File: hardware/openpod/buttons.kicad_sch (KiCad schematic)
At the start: 8 parts

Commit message: update power and audio
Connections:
- net at clickwheel-connector1.1 (VDD): now also MPR1.20 (VDD); no longer MPR1.7 (REXT)
- net at clickwheel-connector1.2 (IRQ): now also MPR1.1 (~{IRQ}); no longer MPR1.6 (VSS)
- net at clickwheel-connector1.3 (SCL): now also MPR1.2 (SCL); no longer MPR1.5 (VREG)
- net at clickwheel-connector1.4 (SDA): now also MPR1.3 (SDA); no longer MPR1.4 (ADDR)
- net at clickwheel-connector1.5 (ADDR): now also MPR1.4 (ADDR); no longer MPR1.3 (SDA)
- net at clickwheel-connector1.6 (VREG): now also MPR1.5 (VREG); no longer MPR1.2 (SCL)
- net at clickwheel-connector1.7 (VSS): now also MPR1.6 (VSS); no longer MPR1.1 (~{IRQ})
- net at clickwheel-connector1.8 (REXT): now also MPR1.7 (REXT); no longer MPR1.20 (VDD)

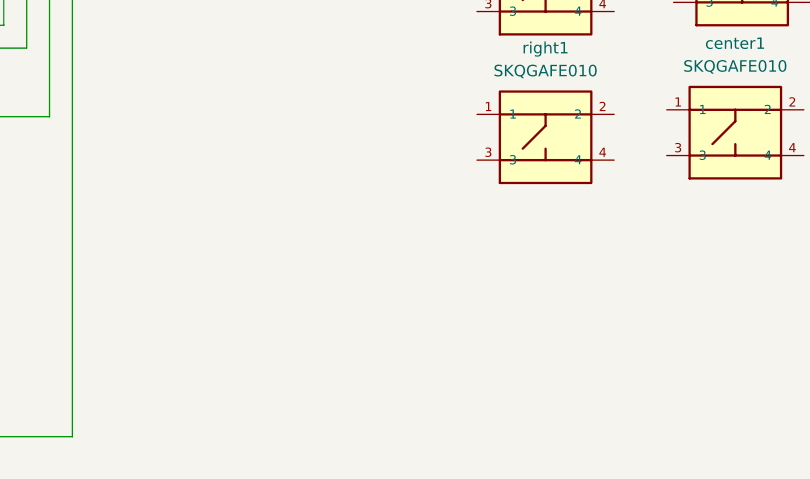
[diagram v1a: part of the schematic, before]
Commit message: added bluetooth
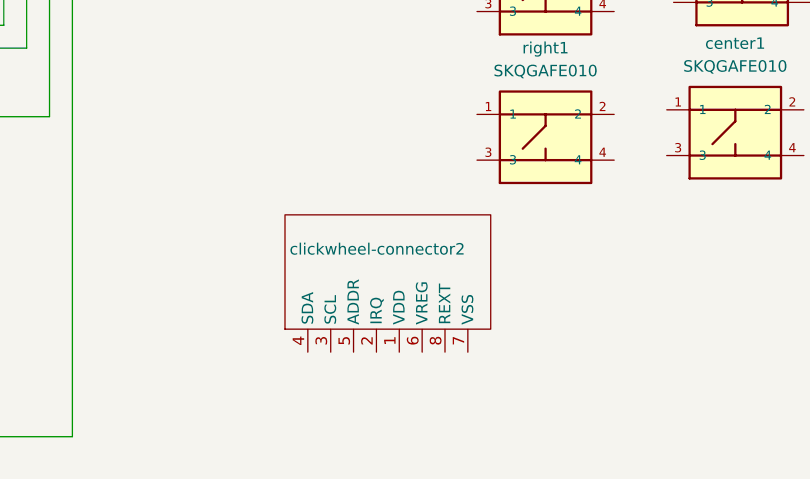
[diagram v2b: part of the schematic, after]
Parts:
- added clickwheel-connector2: ~, Connector_FFC-FPC:Hirose_FH12-8S-0.5SH_1x08-1MP_P0.50mm_Horizontal, symbol openpod:clickwheel-connector
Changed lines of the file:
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@@
+    )
+  )
+  (symbol (lib_id "openpod:clickwheel-connector") (at 123.19 74.422 90) (unit 1)
+    (in_bom yes) (on_board yes) (dnp no)
+    (property "Reference" "clickwheel-connector2" (at 114.808 71.882 90)
+      (effects (font (size 1.27 1.27)) (justify right))
+    )
+    (property "Value" "~" (at 123.19 74.422 0)
+      (effects (font (size 1.27 1.27)))
+    )
+    (property "Footprint" "Connector_FFC-FPC:Hirose_FH12-8S-0.5SH_1x08-1MP_P0.50mm_Horizontal" (at 123.19 74.422 0)
+      (effects (font (size 1.27 1.27)) hide)
+    )
+    (property "Datasheet" "" (at 123.19 74.422 0)
+      (effects (font (size 1.27 1.27)) hide)
+    )
+    (property "Manufacturer" "" (at 123.19 74.422 0)
+      (effects (font (size 1.27 1.27)) hide)
+    )
+    (property "Part number" "" (at 123.19 74.422 0)
+      (effects (font (size 1.27 1.27)) hide)
+    )
+    (property "Supplier" "" (at 123.19 74.422 0)
+      (effects (font (size 1.27 1.27)) hide)
+    )
+    (property "Supplier Part number" "" (at 123.19 74.422 0)
+      (effects (font (size 1.27 1.27)) hide)
+    )
+    (pin "2")
+    (pin "3")
+    (pin "6")
+    (pin "7")
+    (pin "8")
+    (pin "4")
+    (pin "5")
+    (pin "1")
+    (instances
+      (project "openpod"
+        (path "/0122bb8c-dbef-4db1-a6c6-9be780a38d9f/a2d473bc-020f-4f45-b688-c249a4b738f4"
+          (reference "clickwheel-connector2") (unit 1)
+        )
+      )
     )
   )
